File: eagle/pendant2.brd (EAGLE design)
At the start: 15.2 x 34.3 mm, 7 parts, among them U1 ATTINY85-20PU

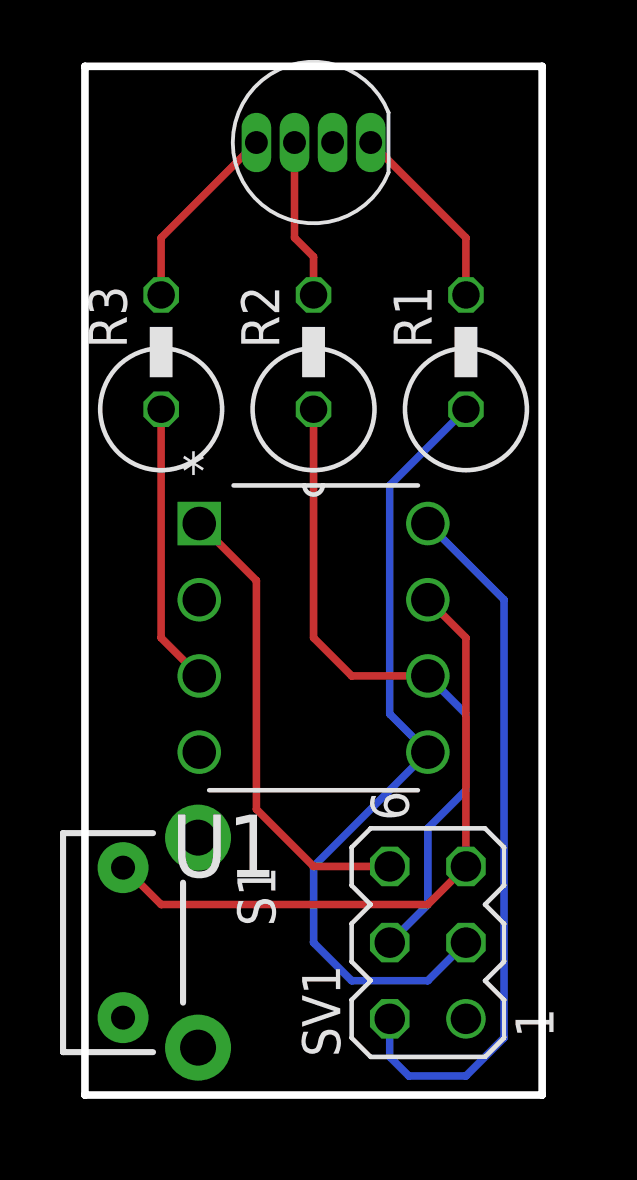
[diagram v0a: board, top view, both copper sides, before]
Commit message: Board slightly reduced in size, silkscreen improved
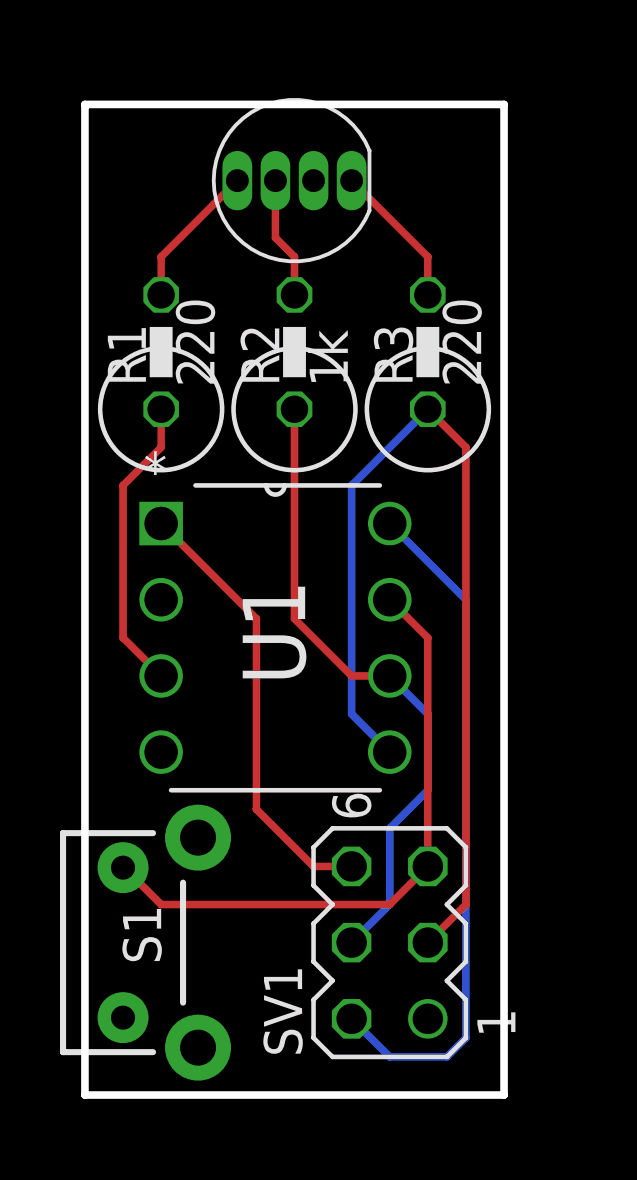
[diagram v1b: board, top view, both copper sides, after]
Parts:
- moved D1 1.42 mm to (6.99, 35.6)
- moved R1 1.27 mm to (11.4, 30.5)
- moved SV1 1.27 mm to (10.2, 10.2)
- moved U1 1.27 mm to (10.2, 16.5)
- moved R2 0.63 mm to (6.99, 30.5)
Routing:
- net ICSP1: track 27.1 -> 31.8 mm
- net N$1: track 6.40 -> 4.86 mm
- net N$3: track 6.40 -> 4.86 mm
- net VCC: track 24.1 -> 22.8 mm
- net ICSP3: track 21.9 -> 20.6 mm
- net N$2: track 5.34 -> 4.07 mm
- net ICSP2: track 22.4 -> 21.4 mm
- net ICSP4: track 15.5 -> 14.8 mm
- net BLUE: track 9.42 -> 9.94 mm
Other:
- board size 15.2 x 34.3 mm -> 14 x 33 mm

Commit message: Made the board yet smaller
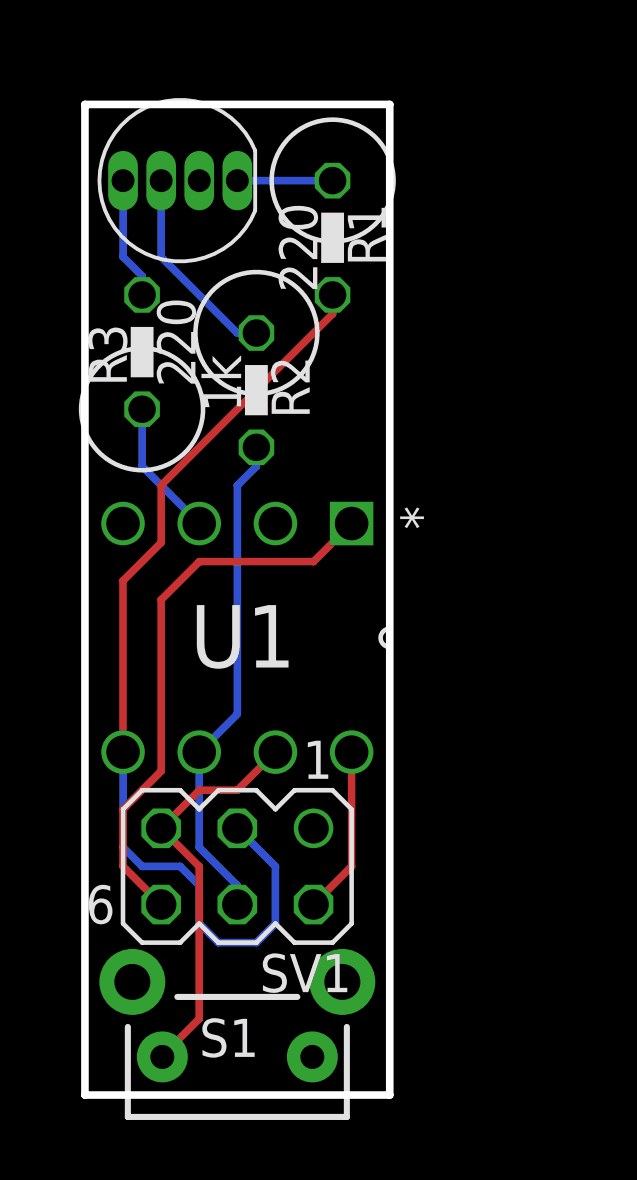
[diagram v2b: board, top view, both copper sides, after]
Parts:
- moved U1 8.89 mm to (1.27, 16.5), turned to 270 degrees
- moved SV1 5.68 mm to (5.08, 12.7), turned to 180 degrees
- moved S1 5.39 mm to (5.08, 6.35), turned to 0 degrees
- moved R1 4.07 mm to (8.26, 33.0), turned to 270 degrees
- moved D1 3.81 mm to (3.17, 35.6)
- moved R2 2.84 mm to (5.71, 27.9), turned to 270 degrees
- moved R3 0.64 mm to (1.91, 30.5)
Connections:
- net ICSP1: now also R1.2; no longer R1.1
- net ICSP2: now also R2.2; no longer R2.1
- net N$1: now also R1.1; no longer R1.2
- net N$2: now also R2.1; no longer R2.2
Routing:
- net VCC: track 22.8 -> 5.61 mm
- net ICSP3: track 20.6 -> 13.5 mm
- net BLUE: track 9.94 -> 4.60 mm
- net ICSP2: track 21.4 -> 16.6 mm
- net ICSP4: track 14.8 -> 18.6 mm
- net N$2: track 4.07 -> 6.77 mm
- net N$1: track 4.86 -> 3.18 mm
- net N$3: track 4.86 -> 4.07 mm
- net ICSP1: track 31.8 -> 32.4 mm
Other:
- board size 14 x 33 mm -> 10.2 x 33 mm
